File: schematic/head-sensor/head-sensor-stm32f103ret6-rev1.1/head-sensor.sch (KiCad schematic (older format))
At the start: 49 parts, among them P1 MICROSD-SDIO-CD, P10 SensorsIn, P11 USART1, P12 SensorsGND, P13 RFID-RC522-MODULE, P14 NRF24L01, P15 HeadLEDs, P16 Power, P2 Vibroengines, P3 NRST, P4 SWGND, P5 VibroenginesVCC, P6 USART3, P7 SWDIO, P8 SWCLK, P9 SensorsVcc, Q1 MOSFET_N, Q2 MOSFET_N, Q3 MOSFET_N, Q4 MOSFET_N, Q5 MOSFET_N, Q6 MOSFET_N, Q7 MOSFET_N, Q8 MOSFET_N, Q9 MOSFET_N, U1 LINSTAB-(1-GND/ADJ,2-OUT,3-IN), U2 STM32F103RE, X1 CRYSTAL

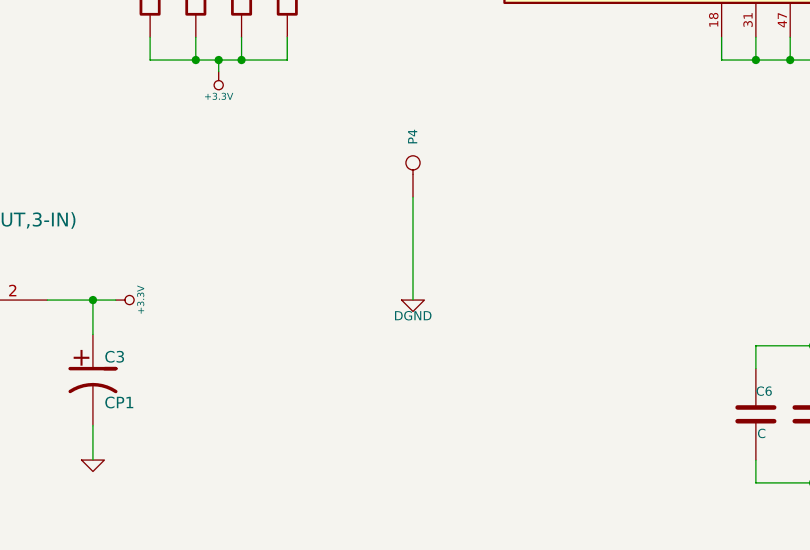
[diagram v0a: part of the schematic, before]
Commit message: Head sensor routing done
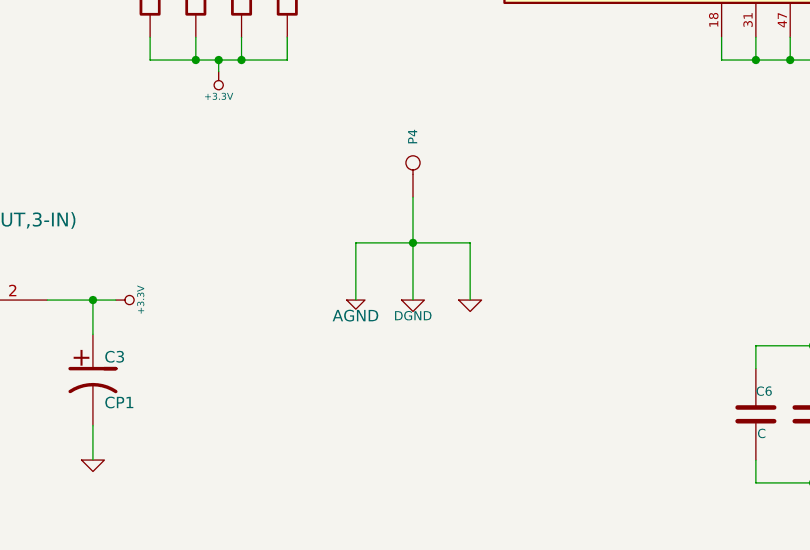
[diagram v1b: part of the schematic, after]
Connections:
- net DGND is gone; now on net AGND: C10.2, C2.1, C4.2, C5.2, C6.2, C7.2, C8.2, C9.2, JP1.1, JP2.1, JP3.1, P1.6 (GND), P1.CD1, P11.1 (P1), P12.1, P12.2, P12.3, P12.4, P12.5, P12.6, P13.6 (GND), P14.1 (GND), P4.1, P6.1 (P1), U2.12 (VSSA), U2.18 (VSS), U2.31 (VSS), U2.47 (VSS), U2.63 (VSS)
- net GND is gone; now on net AGND: C1.2, C3.2, U1.1 (GND/Adj)
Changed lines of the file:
@@
 Sheet 1 1
 Title "Lazertag head sensor"
-Date "15 feb 2015"
+Date "16 feb 2015"
 Rev "1"
 Comp ""
@@
 	1    0    0    -1
 $EndComp
+$Comp
+L GND #PWR?
+U 1 1 54E1E80D
+P 4050 6750
+F 0 "#PWR?" H 4050 6750 30  0001 C CNN
+F 1 "GND" H 4050 6680 30  0001 C CNN
+F 2 "" H 4050 6750 60  0000 C CNN
+F 3 "" H 4050 6750 60  0000 C CNN
+	1    4050 6750
+	1    0    0    -1
+$EndComp
+$Comp
+L AGND #PWR?
+U 1 1 54E1E81C
+P 3550 6750
+F 0 "#PWR?" H 3550 6750 40  0001 C CNN
+F 1 "AGND" H 3550 6680 50  0000 C CNN
+F 2 "" H 3550 6750 60  0000 C CNN
+F 3 "" H 3550 6750 60  0000 C CNN
+	1    3550 6750
+	1    0    0    -1
+$EndComp
+Wire Wire Line
+	3550 6500 4050 6500
+Wire Wire Line
+	4050 6500 4050 6750
+Connection ~ 3800 6500
+Wire Wire Line
+	3550 6750 3550 6500
 $EndSCHEMATC
